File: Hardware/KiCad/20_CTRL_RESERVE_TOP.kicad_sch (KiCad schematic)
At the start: 0 parts

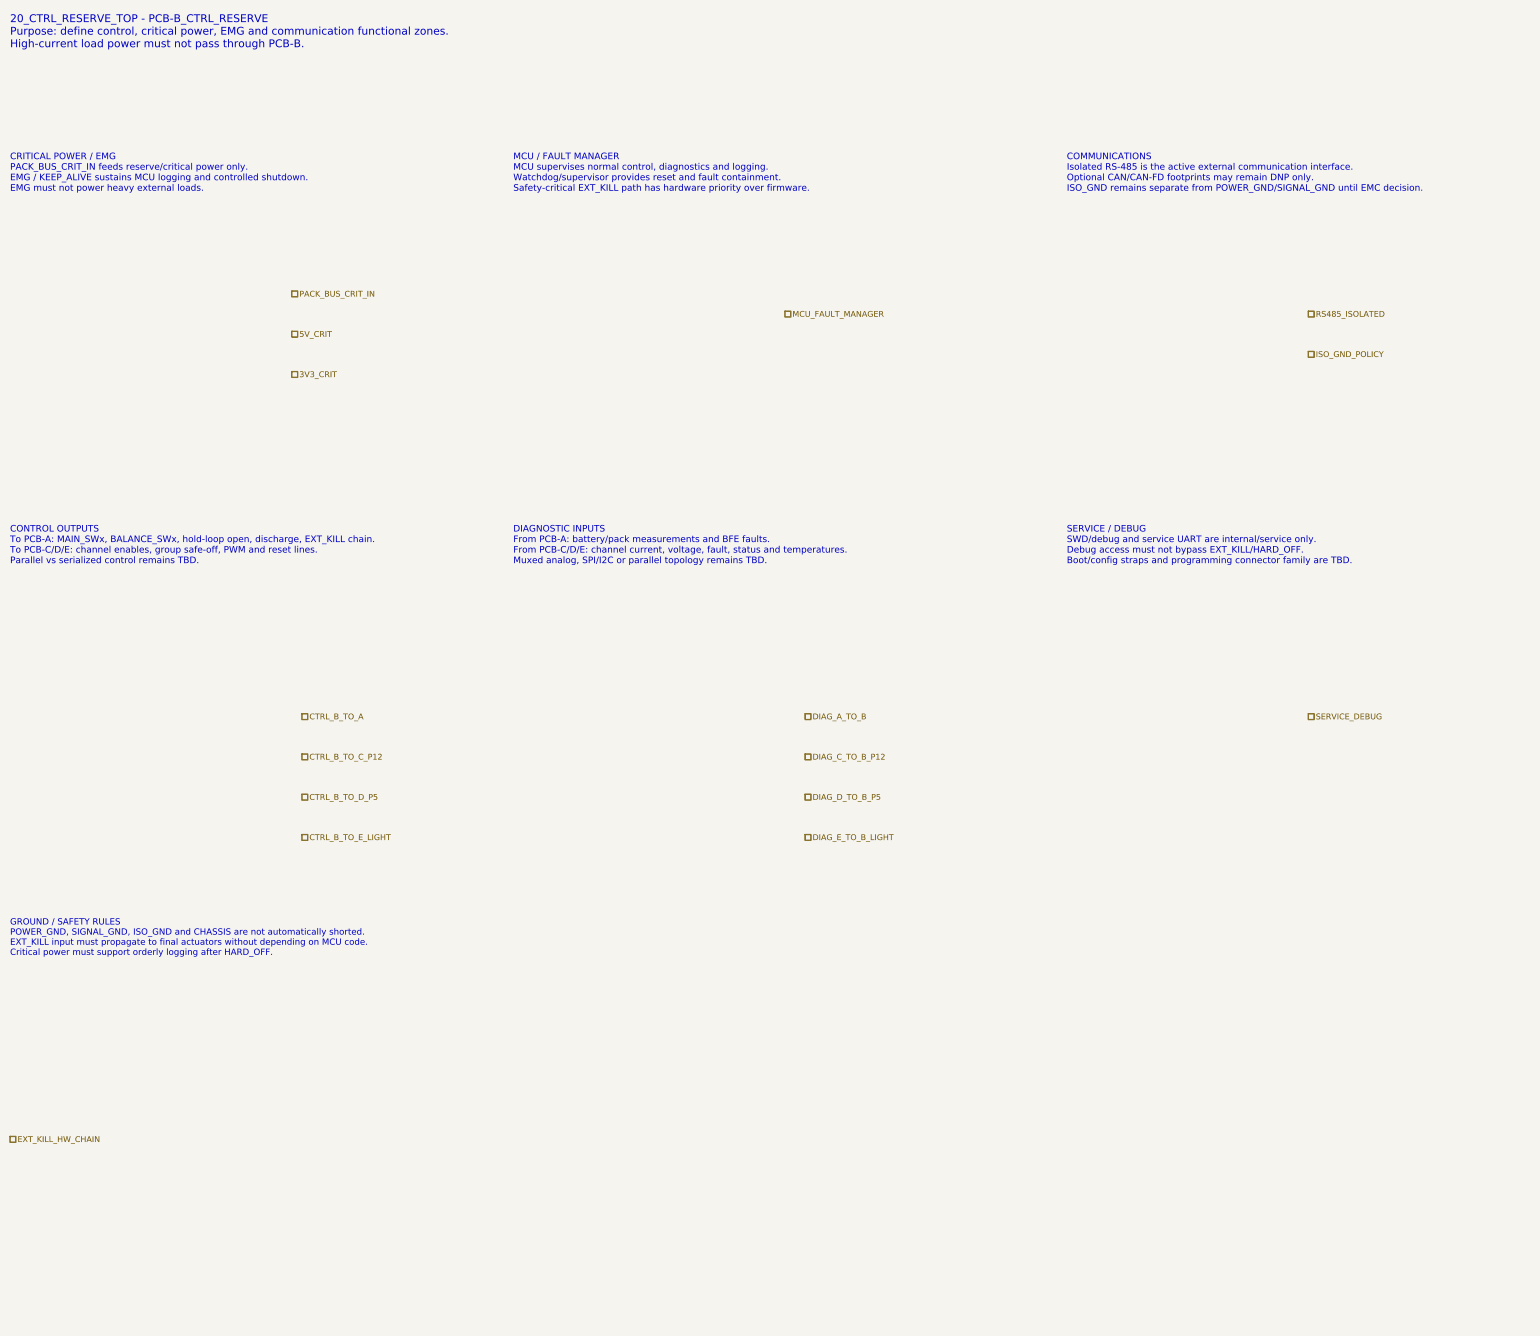
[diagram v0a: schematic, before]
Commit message: hardware: map PCB-B control reserve hierarchy
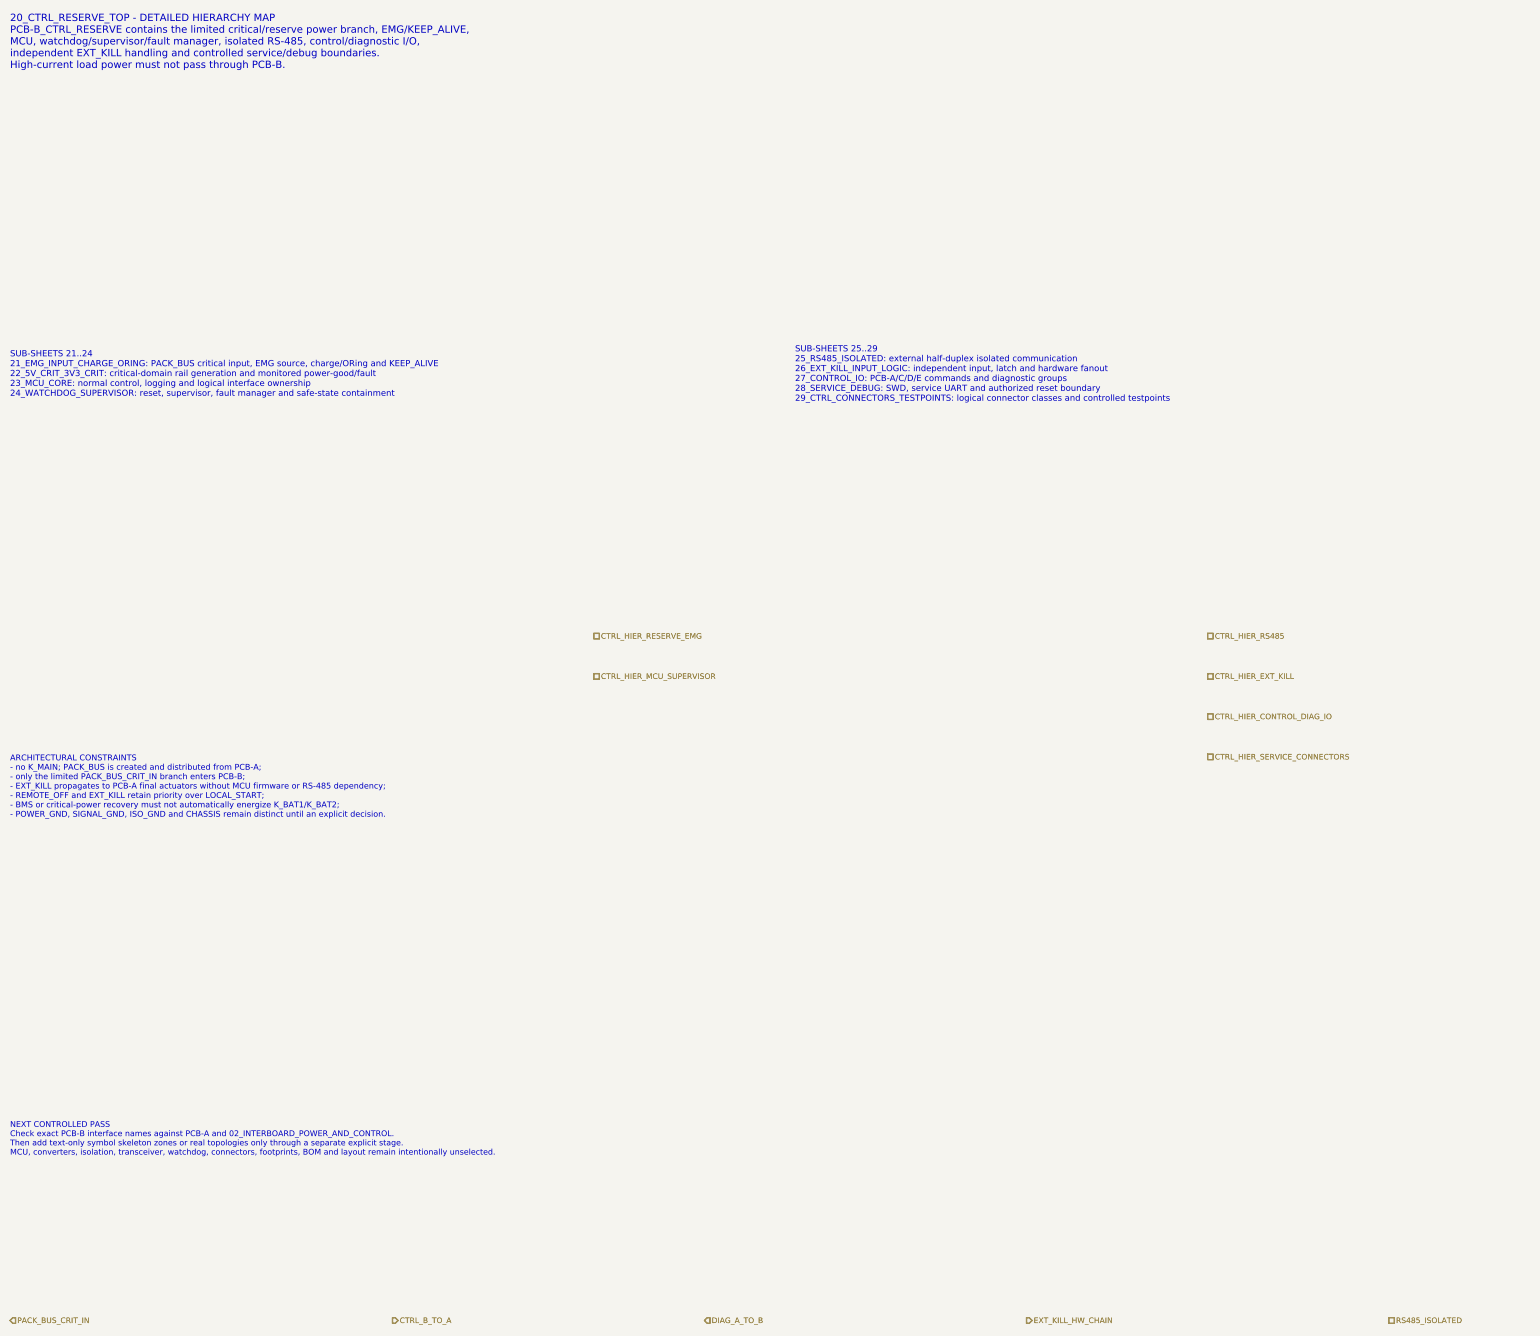
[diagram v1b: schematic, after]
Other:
- note added: "20_CTRL_RESERVE_TOP - DETAILED HIERARCHY MAP PCB-B_CTRL_RESERVE contains the limited critical/reserve power branch, EMG/KEEP_ALIVE, MCU, watchdog/supervisor/fault manager, isolated RS-485, control/diagnostic I/O, independent EXT_KILL handling and controlled service/debug boundaries. High-current load power must not pass through PCB-B."
- note added: "ARCHITECTURAL CONSTRAINTS - no K_MAIN; PACK_BUS is created and distributed from PCB-A; - only the limited PACK_BUS_CRIT_IN branch enters PCB-B; - EXT_KILL propagates to PCB-A final actuators without MCU firmware or RS-485 dependency; - REMOTE_OFF and EXT_KILL retain priority over LOCAL_START; - BMS or critical-power recovery must not automatically energize K_BAT1/K_BAT2; - POWER_GND, SIGNAL_GND, 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"
- note added: "NEXT CONTROLLED PASS Check exact PCB-B interface names against PCB-A and 02_INTERBOARD_POWER_AND_CONTROL. Then add text-only symbol skeleton zones or real topologies only through a separate explicit stage. MCU, converters, isolation, transceiver, watchdog, connectors, footprints, BOM and layout remain intentionally unselected."
- note added: "SUB-SHEETS 21..24 21_EMG_INPUT_CHARGE_ORING: PACK_BUS critical input, EMG source, charge/ORing and KEEP_ALIVE 22_5V_CRIT_3V3_CRIT: critical-domain rail generation and monitored power-good/fault 23_MCU_CORE: normal control, logging and logical interface ownership 24_WATCHDOG_SUPERVISOR: reset, supervisor, fault manager and safe-state containment"
- note added: "SUB-SHEETS 25..29 25_RS485_ISOLATED: external half-duplex isolated communication 26_EXT_KILL_INPUT_LOGIC: independent input, latch and hardware fanout 27_CONTROL_IO: PCB-A/C/D/E commands and diagnostic groups 28_SERVICE_DEBUG: SWD, service UART and authorized reset boundary 29_CTRL_CONNECTORS_TESTPOINTS: logical connector classes and controlled testpoints"
- note removed: "20_CTRL_RESERVE_TOP - PCB-B_CTRL_RESERVE Purpose: define control, critical power, EMG and communication functional zones. High-current load power must not pass through PCB-B."
- note removed: "COMMUNICATIONS Isolated RS-485 is the active external communication interface. Optional CAN/CAN-FD footprints may remain DNP only. ISO_GND remains separate from POWER_GND/SIGNAL_GND until EMC decision."
- note removed: "CONTROL OUTPUTS To PCB-A: MAIN_SWx, BALANCE_SWx, hold-loop open, discharge, EXT_KILL chain. To PCB-C/D/E: channel enables, group safe-off, PWM and reset lines. Parallel vs serialized control remains TBD."
- note removed: "CRITICAL POWER / EMG PACK_BUS_CRIT_IN feeds reserve/critical power only. EMG / KEEP_ALIVE sustains MCU logging and controlled shutdown. EMG must not power heavy external loads."
- note removed: "DIAGNOSTIC INPUTS From PCB-A: battery/pack measurements and BFE faults. From PCB-C/D/E: channel current, voltage, fault, status and temperatures. Muxed analog, SPI/I2C or parallel topology remains TBD."
- note removed: "GROUND / SAFETY RULES POWER_GND, SIGNAL_GND, ISO_GND and CHASSIS are not automatically shorted. EXT_KILL input must propagate to final actuators without depending on MCU code. Critical power must support orderly logging after HARD_OFF."
- note removed: "MCU / FAULT MANAGER MCU supervises normal control, diagnostics and logging. Watchdog/supervisor provides reset and fault containment. Safety-critical EXT_KILL path has hardware priority over firmware."
- note removed: "SERVICE / DEBUG SWD/debug and service UART are internal/service only. Debug access must not bypass EXT_KILL/HARD_OFF. Boot/config straps and programming connector family are TBD."
